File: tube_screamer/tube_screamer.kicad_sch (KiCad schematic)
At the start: 68 parts, among them J1 Jack_6.35, J2 Jack_6.35, J3 Conn_01x05, J4 Conn_01x05, J5 Conn_01x05, J6 Barrel_Jack_Switch, J7 Conn_01x01_Socket, J8 Conn_01x01_Socket, P1 tube_screamer_front_panel, Q1 MMBT5551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

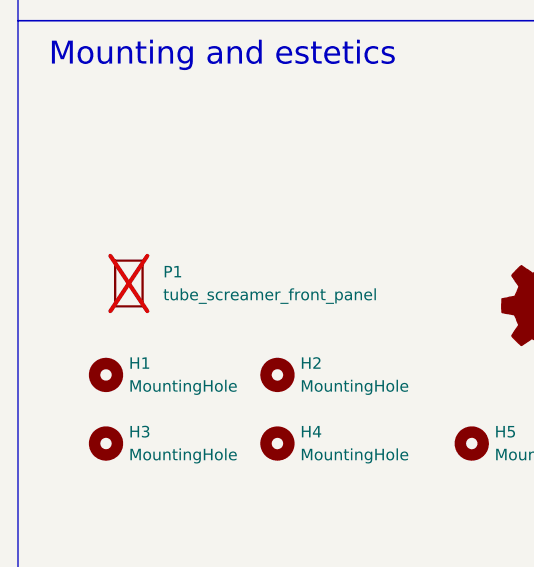
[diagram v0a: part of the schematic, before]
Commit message: Pots fit, battery holder has to be moved.
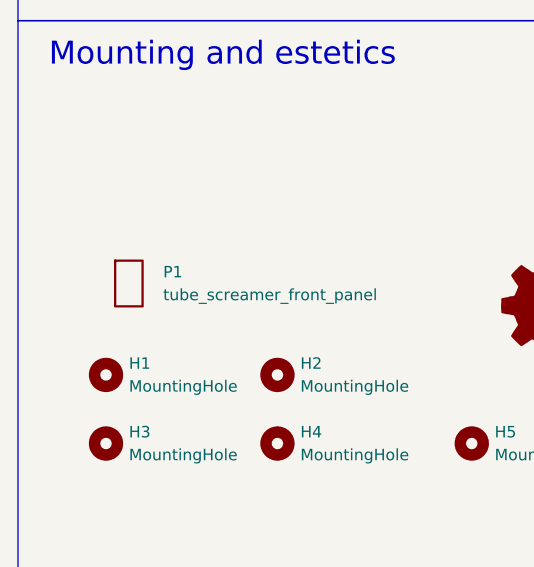
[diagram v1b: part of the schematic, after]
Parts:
- P1: now fitted
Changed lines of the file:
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@@
 		(in_bom yes)
 		(on_board yes)
-		(dnp yes)
+		(dnp no)
 		(fields_autoplaced yes)
 		(property "Reference" "P1"

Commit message: Updated, added 3d bodies.
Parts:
- added P2: bottom_plate, pedale:bottom_plate, symbol pedale:tube_screamer_front_panel
- P1: value tube_screamer_front_panel -> front_plate; footprint pedale:tube_screamer_front_plate -> pedale:front_plate
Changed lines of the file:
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@@
+	)
+	(symbol
+		(lib_id "pedale:tube_screamer_front_panel")
+		(at 40.64 109.22 0)
+		(unit 1)
+		(exclude_from_sim no)
+		(in_bom yes)
+		(on_board yes)
+		(dnp no)
+		(fields_autoplaced yes)
+		(property "Reference" "P2"
+			(at 43.18 107.9499 0)
+			(effects
+				(font
+					(size 1.27 1.27)
+				)
+				(justify left)
+			)
+		)
+		(property "Value" "bottom_plate"
+			(at 43.18 110.4899 0)
+			(effects
+				(font
+					(size 1.27 1.27)
+				)
+				(justify left)
+			)
+		)
+		(property "Footprint" "pedale:bottom_plate"
+			(at 40.64 109.22 0)
+			(effects
+				(font
+					(size 1.27 1.27)
+				)
+				(hide yes)
+			)
+		)
+		(property "Datasheet" "~"
+			(at 40.64 109.22 0)
+			(effects
+				(font
+					(size 1.27 1.27)
+				)
+				(hide yes)
+			)
+		)
+		(property "Description" "Potentiometer"
+			(at 40.64 109.22 0)
+			(effects
+				(font
+					(size 1.27 1.27)
+				)
+				(hide yes)
+			)
+		)
+		(instances
+			(project "tube_screamer"
+				(path "/e0801131-6974-42d8-8070-4ed960891aa7"
+					(reference "P2")
+					(unit 1)
+				)
+			)
+		)
 	)
 	(symbol
@@
 		(fields_autoplaced yes)
 		(property "Reference" "P1"
-			(at 27.94 107.9499 0)
+			(at 26.67 107.9499 0)
 			(effects
 				(font
@@
 			)
 		)
-		(property "Value" "tube_screamer_front_panel"
-			(at 27.94 110.4899 0)
+		(property "Value" "front_plate"
+			(at 26.67 110.4899 0)
 			(effects
 				(font
@@
 			)
 		)
-		(property "Footprint" "pedale:tube_screamer_front_plate"
+		(property "Footprint" "pedale:front_plate"
 			(at 24.13 109.22 0)
 			(effects

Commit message: Update schematic.
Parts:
- removed D3, D5: 1N4148WS, Diode_SMD:D_SOD-323, symbol Diode:1N4148WS
- removed D8: floating_green_led, pedale:floating_green_led, symbol pedale:floating_green_led
- removed D9: floating_red_led, pedale:floating_red_led, symbol pedale:floating_red_led
- removed J3, J4, J5: Conn_01x05, Connector_JST:JST_EH_B5B-EH-A_1x05_P2.50mm_Vertical, symbol Connector_Generic:Conn_01x05
- removed R18, R8: 1k, Resistor_SMD:R_0603_1608Metric_Pad0.98x0.95mm_HandSolder, symbol Device:R
- removed RV5, RV6, RV8: floating_pot, pedale:floating_pot, symbol pedale:floating_pot
- added J9: top_panel_connector, Connector_IDC:IDC-Header_2x08_P2.54mm_Vertical, symbol pedale:top_panel_connector
- added Q10, Q6, Q8: AO3401A, Package_TO_SOT_SMD:SOT-23, symbol Transistor_FET:AO3401A
- added Q12, Q13, Q14: AO3400A, Package_TO_SOT_SMD:SOT-23, symbol Transistor_FET:AO3400A
- added R24, R27: 100k, Resistor_SMD:R_0603_1608Metric_Pad0.98x0.95mm_HandSolder, symbol Device:R
- added R26, R28: 1k, Resistor_SMD:R_0603_1608Metric_Pad0.98x0.95mm_HandSolder, symbol Device:R
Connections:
- net 0: now also J9.16 (Pin_16), J9.3 (GND), Q12.2 (S), Q13.2 (S), Q14.2 (S); no longer J1.R, J2.R, J6.2
- net 9V: now also SW1.4 (A), J9.1 (VCC), R26.2; no longer SW1.6 (C)
- net OP_OUT: now also J9.12 (Pin_12)
- net SW_ON: now also J9.14 (Pin_14)
- net REG_IN: now reaches Q3.3 (C), R16.2
- net REG_IN: now also Q10.2 (S), Q6.2 (S), Q8.2 (S)
- net at R47.2: now also J9.6 (Pin_6)
- net at C3.2, D1.2 (A), D2.1 (K)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: now also J9.2 (Pin_2), J9.4 (Pin_4)
- net BAT+: now reaches BT1.1 (+), J7.1 (Pin_1)
- net BAT+: now also Q6.3 (D), R24.1, R27.1
- net at C4.2, R25.1, R4.1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: now also J9.9 (Pin_9)
- net CONN+: now reaches J6.1
- net CONN+: now also Q10.1 (G), Q13.3 (D), Q14.1 (G), Q8.3 (D)
- net BAT-: now reaches BT1.2 (-), J6.3, J8.1 (Pin_1)
- net at SW1.5 (B): now also R28.2
- net at R6.2, U1.6 (-): now also J9.5 (Pin_5)
- net at C6.1: now also J9.7 (Pin_7)
- new net: Q12.3 (D), Q6.1 (G), R24.2
- new net: J9.8 (Pin_8), R28.1
- new net: J9.10 (Pin_10), R26.1
- new net CONN-: J6.2, Q10.3 (D), Q13.1 (G), Q14.3 (D), Q8.1 (G)
- new net IN_CONNECT: Q12.1 (G), R27.2
- no-connect marks 3 -> 4
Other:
- moved on the sheet: BT1, C6, C7, J7, J8, R14, R25, R47, R6, R7, SW1B, U1B

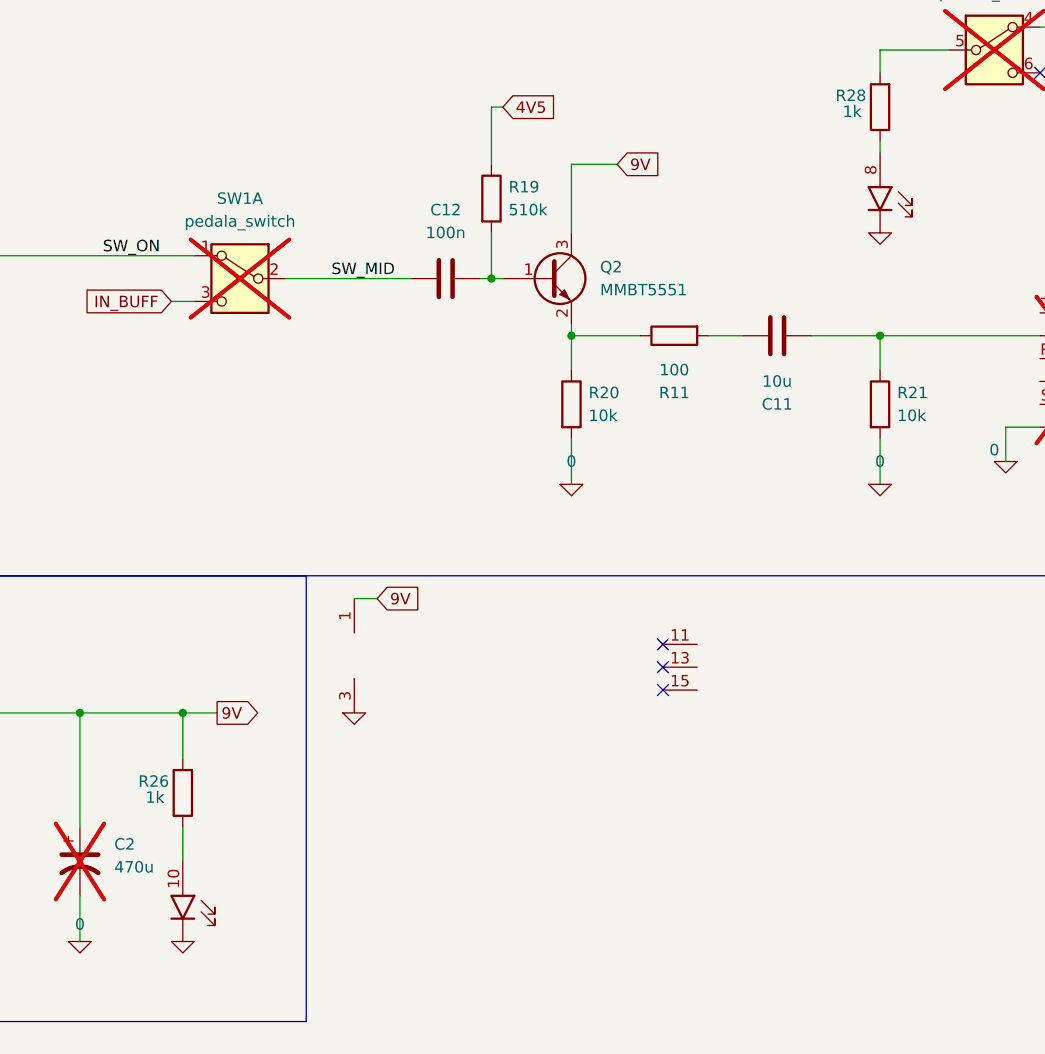
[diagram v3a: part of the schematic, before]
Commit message: 1 Red, 3 green connector.
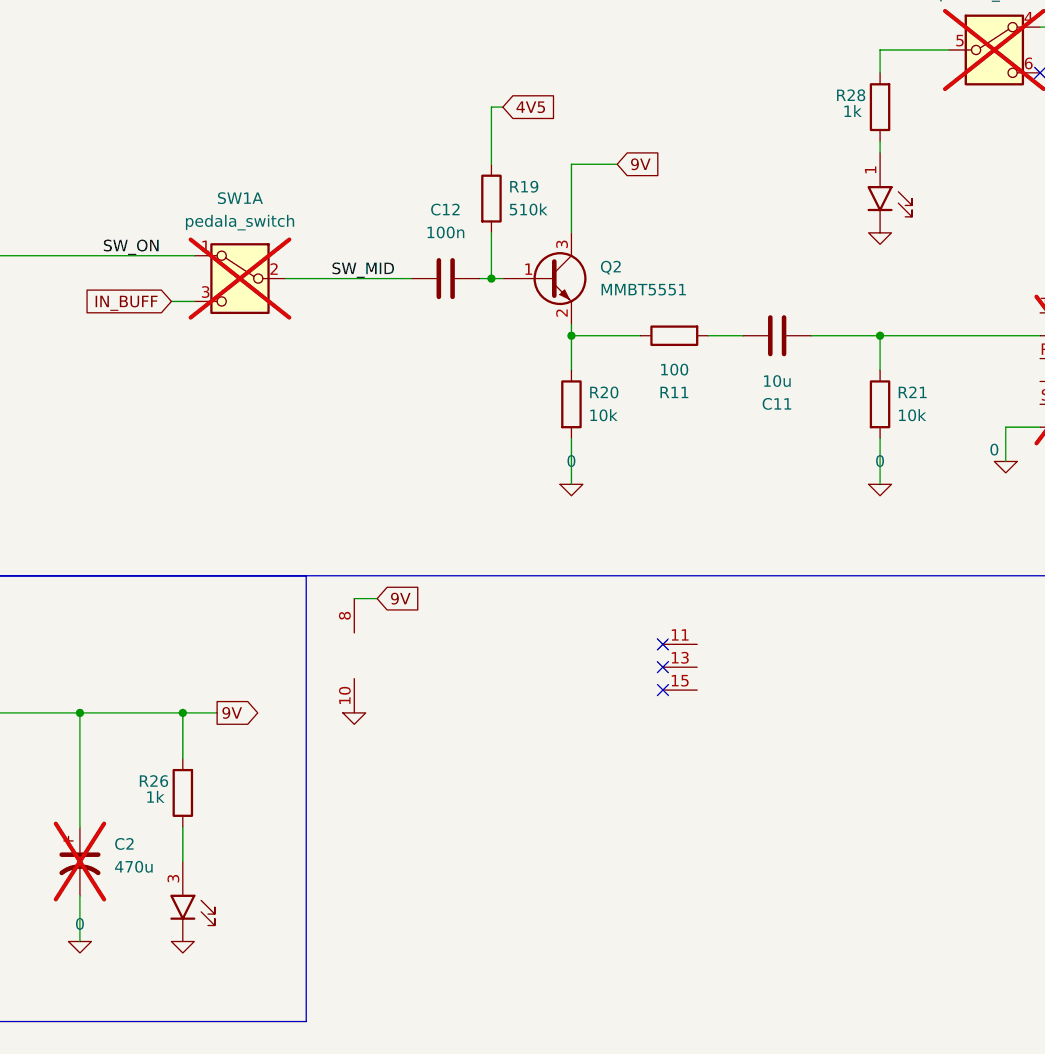
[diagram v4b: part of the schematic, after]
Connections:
- net 0: now also J9.10 (GND); no longer J9.3 (GND)
- net 9V: now also J9.8 (VCC); no longer J9.1 (VCC)
- net at R28.1: now also J9.1 (Pin_8); no longer J9.8 (Pin_8)
- net at R26.1: now also J9.3 (1); no longer J9.10 (Pin_10)
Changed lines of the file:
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@@
 	)
 	(symbol
+		(lib_name "MountingHole_1")
 		(lib_id "Mechanical:MountingHole")
 		(at 21.59 127 0)
@@
 	)
 	(symbol
+		(lib_name "0_5")
 		(lib_id "Simulation_SPICE:0")
 		(at 111.76 189.23 0)
@@
 	)
 	(symbol
+		(lib_name "BC817_1")
 		(lib_id "Transistor_BJT:BC817")
 		(at 111.76 166.37 90)
@@
 	)
 	(symbol
+		(lib_name "0_4")
 		(lib_id "Simulation_SPICE:0")
 		(at 240.03 53.34 0)
@@
 	)
 	(symbol
+		(lib_name "BC817_2")
 		(lib_id "Transistor_BJT:BC817")
 		(at 203.2 115.57 0)
@@
 	)
 	(symbol
+		(lib_name "0_2")
 		(lib_id "Simulation_SPICE:0")
 		(at 105.41 261.62 0)
@@
 	)
 	(symbol
+		(lib_name "0_11")
 		(lib_id "Simulation_SPICE:0")
 		(at 99.06 189.23 0)
@@
 	)
 	(symbol
+		(lib_name "0_10")
 		(lib_id "Simulation_SPICE:0")
 		(at 172.72 73.66 0)
@@
 	)
 	(symbol
+		(lib_name "0_18")
 		(lib_id "Simulation_SPICE:0")
 		(at 180.34 54.61 0)
@@
 	)
 	(symbol
+		(lib_name "MountingHole_3")
 		(lib_id "Mechanical:MountingHole")
 		(at 62.23 127 0)
@@
 	)
 	(symbol
+		(lib_name "0_20")
 		(lib_id "Simulation_SPICE:0")
 		(at 125.73 123.19 0)
@@
 	)
 	(symbol
+		(lib_name "0_19")
 		(lib_id "Simulation_SPICE:0")
 		(at 41.91 60.96 0)
@@
 	)
 	(symbol
+		(lib_name "0_3")
 		(lib_id "Simulation_SPICE:0")
 		(at 151.13 189.23 0)
@@
 	)
 	(symbol
+		(lib_name "0_9")
 		(lib_id "Simulation_SPICE:0")
 		(at 138.43 189.23 0)
@@
 	)
 	(symbol
+		(lib_name "0_14")
 		(lib_id "Simulation_SPICE:0")
 		(at 240.03 138.43 0)
@@
 	)
 	(symbol
+		(lib_name "MountingHole_2")
 		(lib_id "Mechanical:MountingHole")
 		(at 21.59 119.38 0)
@@
 	)
 	(symbol
+		(lib_name "0_8")
 		(lib_id "Simulation_SPICE:0")
 		(at 85.09 189.23 0)
@@
 	)
 	(symbol
+		(lib_name "MountingHole_4")
 		(lib_id "Mechanical:MountingHole")
 		(at 40.64 127 0)
@@
 	)
 	(symbol
+		(lib_name "0_13")
 		(lib_id "Simulation_SPICE:0")
 		(at 259.08 53.34 0)
@@
 	)
 	(symbol
+		(lib_name "0_12")
 		(lib_id "Simulation_SPICE:0")
 		(at 57.15 240.03 270)
@@
 	)
 	(symbol
+		(lib_name "0_6")
 		(lib_id "Simulation_SPICE:0")
 		(at 248.92 53.34 0)
@@
 	)
 	(symbol
+		(lib_name "0_1")
 		(lib_id "Simulation_SPICE:0")
 		(at 125.73 189.23 0)
@@
 	)
 	(symbol
+		(lib_name "0_17")
 		(lib_id "Simulation_SPICE:0")
 		(at 118.11 48.26 270)
@@
 	)
 	(symbol
+		(lib_name "0_16")
 		(lib_id "Simulation_SPICE:0")
 		(at 205.74 138.43 0)
@@
 	)
 	(symbol
+		(lib_name "0_15")
 		(lib_id "Simulation_SPICE:0")
 		(at 254 135.89 0)
@@
 	)
 	(symbol
+		(lib_name "0_7")
 		(lib_id "Simulation_SPICE:0")
 		(at 181.61 163.83 0)

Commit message: Pots checked, all good.
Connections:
- no-connect marks 4 -> 12
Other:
- moved on the sheet: P1
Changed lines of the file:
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@@
 	)
 	(no_connect
+		(at 257.81 119.38)
+	)
+	(no_connect
 		(at 215.9 158.75)
 	)
@@
 	)
 	(no_connect
+		(at 257.81 127)
+	)
+	(no_connect
 		(at 215.9 156.21)
 	)
 	(no_connect
+		(at 36.83 49.53)
+	)
+	(no_connect
+		(at 257.81 129.54)
+	)
+	(no_connect
+		(at 36.83 44.45)
+	)
+	(no_connect
+		(at 257.81 124.46)
+	)
+	(no_connect
 		(at 257.81 92.71)
 	)
+	(no_connect
+		(at 36.83 54.61)
+	)
+	(no_connect
+		(at 36.83 52.07)
+	)
 	(wire
 		(pts
@@
 	(symbol
 		(lib_id "pedale:tube_screamer_front_panel")
-		(at 24.13 109.22 0)
+		(at 21.59 109.22 0)
 		(unit 1)
 		(exclude_from_sim no)
@@
 		(fields_autoplaced yes)
 		(property "Reference" "P1"
-			(at 26.67 107.9499 0)
+			(at 24.13 107.9499 0)
 			(effects
 				(font
@@
 		)
 		(property "Value" "front_plate"
-			(at 26.67 110.4899 0)
+			(at 24.13 110.4899 0)
 			(effects
 				(font
@@
 		)
 		(property "Footprint" "pedale:front_plate"
-			(at 24.13 109.22 0)
+			(at 21.59 109.22 0)
 			(effects
 				(font
@@
 		)
 		(property "Datasheet" "~"
-			(at 24.13 109.22 0)
+			(at 21.59 109.22 0)
 			(effects
 				(font
@@
 		)
 		(property "Description" "Potentiometer"
-			(at 24.13 109.22 0)
+			(at 21.59 109.22 0)
 			(effects
 				(font

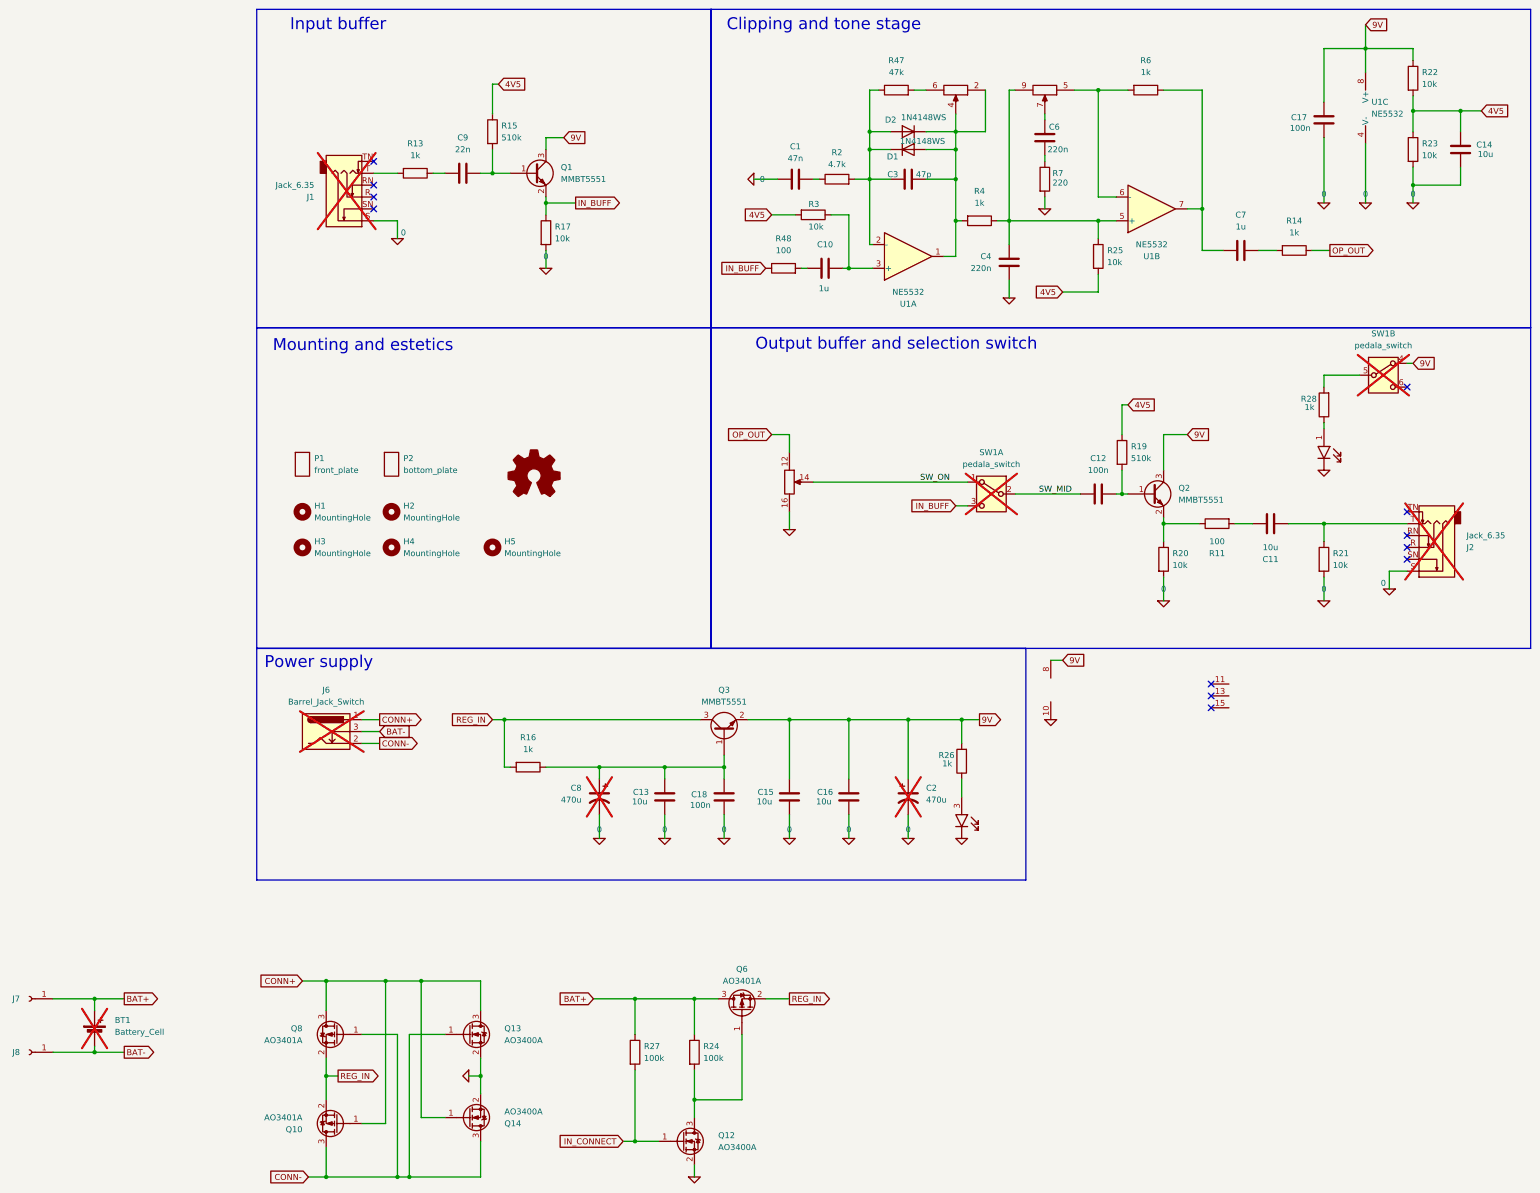
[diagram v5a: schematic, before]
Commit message: Fixed diodes on front plate, fixed power schem.
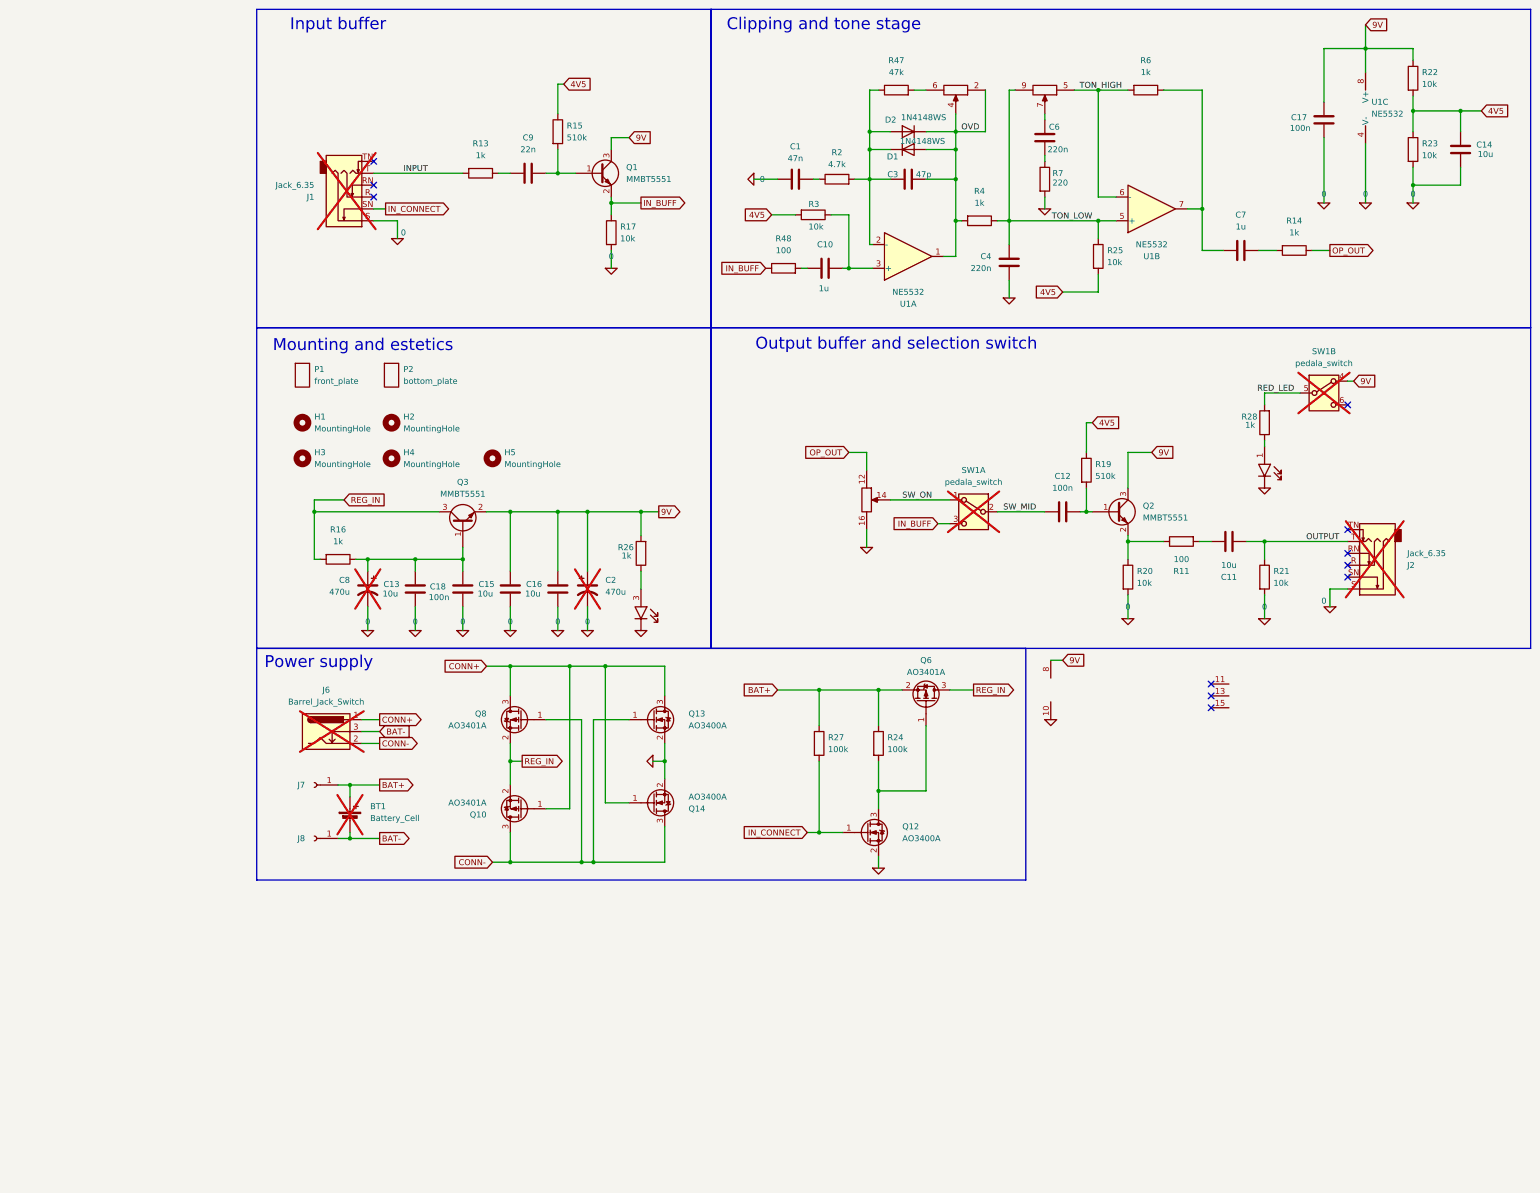
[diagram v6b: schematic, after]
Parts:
- removed SIM1: Logo_Open_Hardware_Small, Symbol:OSHW-Logo2_7.3x6mm_SilkScreen, symbol Graphic:Logo_Open_Hardware_Small
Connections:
- net BAT+: now also Q6.2 (S); no longer Q6.3 (D)
- net IN_CONNECT: now also J1.SN
- net REG_IN: now also Q6.3 (D); no longer Q6.2 (S)
- net OVD: now reaches C3.2, D1.2 (A), D2.1 (K), J9.2 (Pin_2), J9.4 (Pin_4), R4.2, U1.1
- net TON_LOW: now reaches C4.2, J9.9 (Pin_9), R25.1, R4.1, U1.5 (+)
- net RED_LED: now reaches R28.2, SW1.5 (B)
- net TON_HIGH: now reaches J9.5 (Pin_5), R6.2, U1.6 (-)
- net OUTPUT: now reaches C11.2, J2.T, R21.1
- net INPUT: now reaches J1.T, R13.2
- no-connect marks 12 -> 11
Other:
- moved on the sheet: BT1, C11, C12, C13, C15, C16, C18, C2, C8, C9, H1, H2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
